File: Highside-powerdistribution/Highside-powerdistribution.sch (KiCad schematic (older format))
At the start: 43 parts, among them J1 Conn_01x02_Male, J10 Screw_Terminal_01x02, J11 Screw_Terminal_01x02, J12 Screw_Terminal_01x02, J13 Screw_Terminal_01x02, J14 Conn_01x02, J15 Screw_Terminal_01x06, J2 Conn_01x02_Male, J3 Conn_01x02_Male, J4 Conn_01x02_Male, J5 Conn_01x02_Male, J8 Screw_Terminal_01x02, J9 Screw_Terminal_01x02, Q1 P-MOSFET, Q2 P-MOSFET, Q3 P-MOSFET, Q4 P-MOSFET, Q5 P-MOSFET, Q6 P-MOSFET

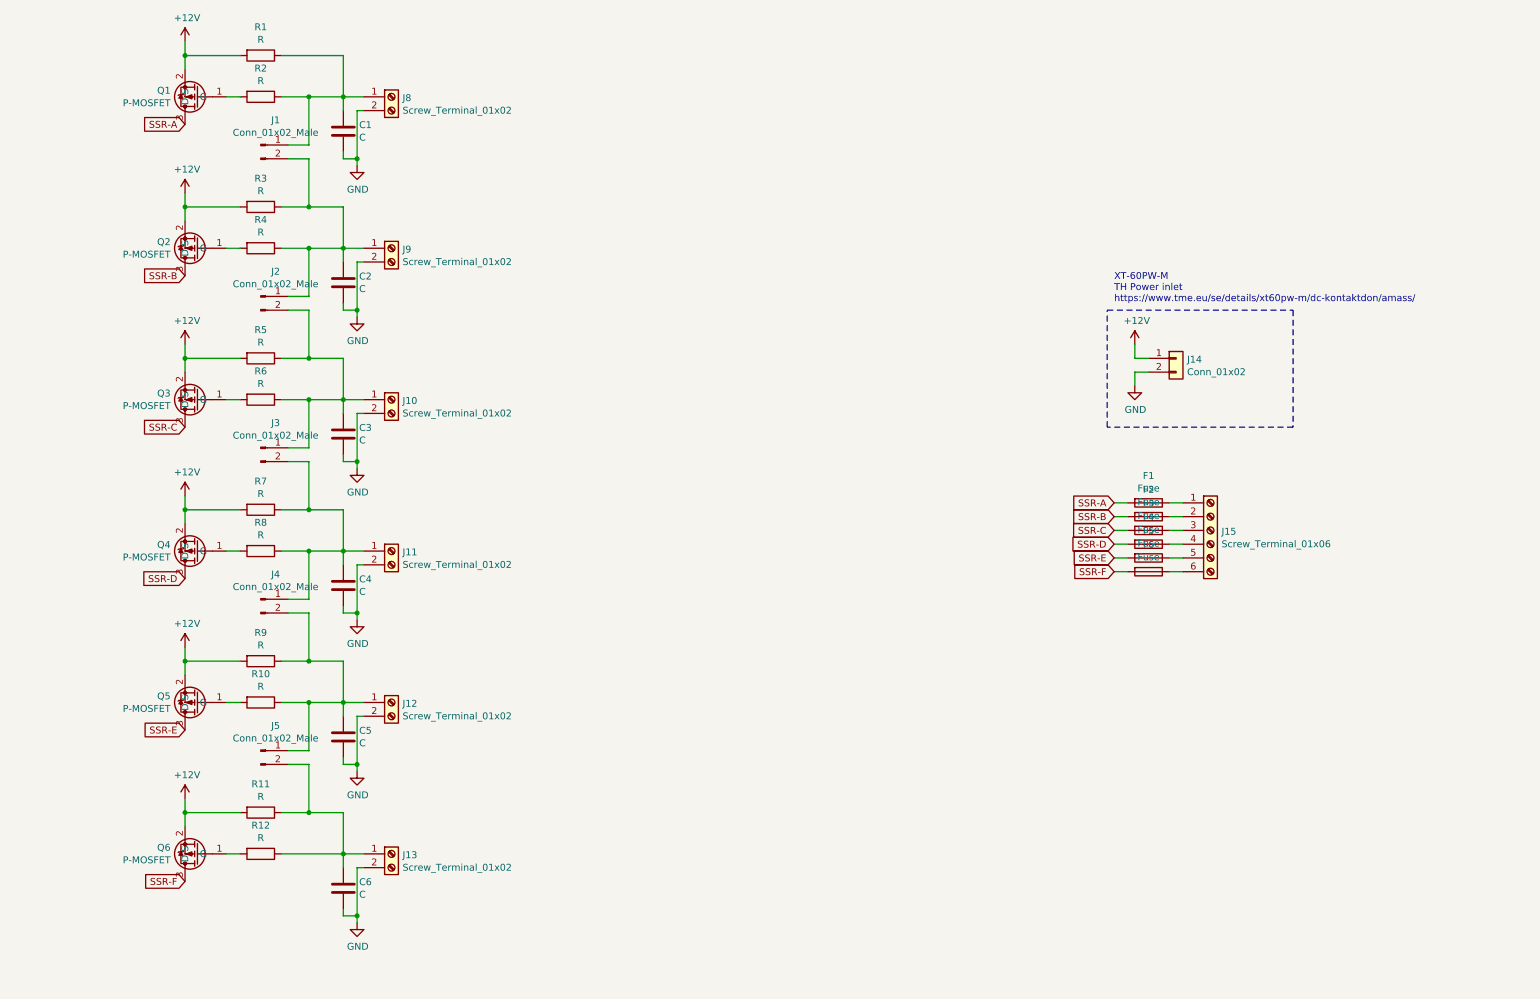
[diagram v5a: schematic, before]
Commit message: Moved resistor to create LP-filter from switch.
Instead of a useless resistor on gate, now in LP-filter from switch.
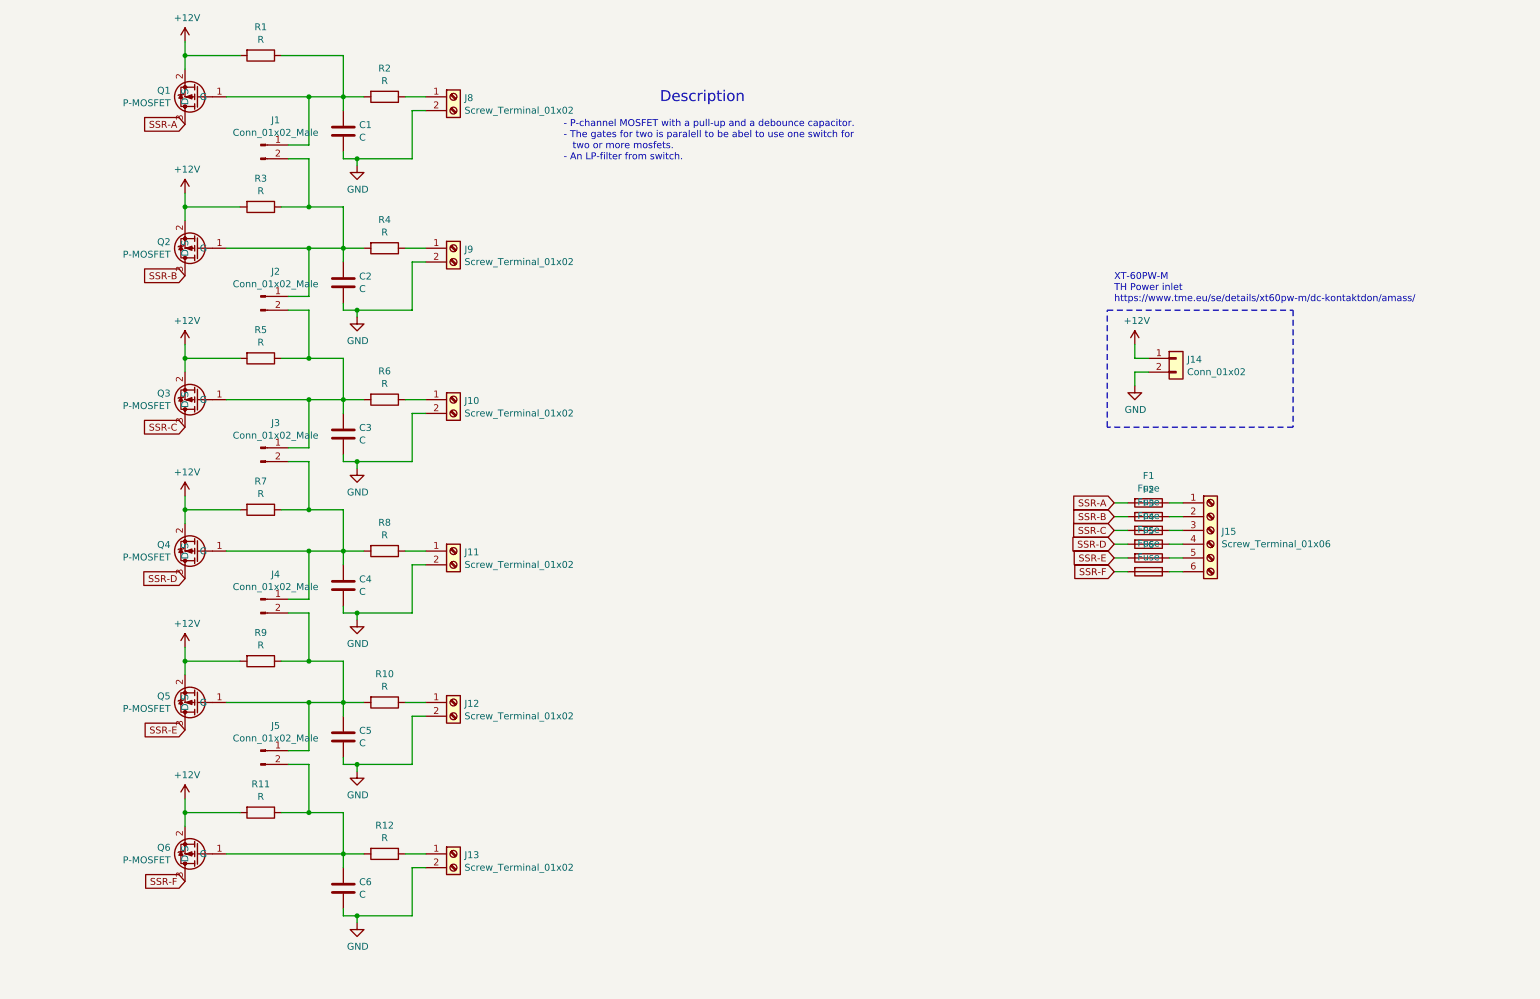
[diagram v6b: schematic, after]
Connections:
- net at Q1.1 (G), R2.2: now also C1.1, J1.1 (Pin_1), R1.1
- net at Q2.1 (G), R4.2: now also C2.1, J1.2 (Pin_2), J2.1 (Pin_1), R3.1
- net at Q3.1 (G), R6.2: now also C3.1, J2.2 (Pin_2), J3.1 (Pin_1), R5.1
- net at Q4.1 (G), R8.2: now also C4.1, J3.2 (Pin_2), J4.1 (Pin_1), R7.1
- net at Q5.1 (G), R10.2: now also C5.1, J4.2 (Pin_2), J5.1 (Pin_1), R9.1
- net at C6.1, J5.2 (Pin_2), R11.1: now also Q6.1 (G), R12.2; no longer J13.1 (Pin_1), R12.1
- new net: J8.1 (Pin_1), R2.1
- new net: J13.1 (Pin_1), R12.1
- new net: J9.1 (Pin_1), R4.1
- new net: J10.1 (Pin_1), R6.1
- new net: J11.1 (Pin_1), R8.1
- new net: J12.1 (Pin_1), R10.1
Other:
- note added: "- P-channel MOSFET with a pull-up and a debounce capacitor. \n- The gates for two is paralell to be abel to use one switch for \n two or more mosfets.\n- An LP-filter from switch. \n\n"
- note added: "Description"
- moved on the sheet: J10, J11, J12, J13, J8, J9, R10, R12, R2, R4, R6, R8
